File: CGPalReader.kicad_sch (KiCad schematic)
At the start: 27 parts, among them J1 Conn_01x06, U1 74LS14, U2 74LS393, U3 74LS393, U4 74LS151, U5 74LS393, U6 74LS151, U7 74LS157, U8 PAL16L8, U9 PAL20L10

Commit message: Add files via upload
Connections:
- net GND: now also U6.1 (I3), U6.12 (I7), U6.13 (I6), U6.14 (I5), U6.15 (I4)
- no-connect marks 21 -> 16
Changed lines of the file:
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@@
   (junction (at 109.22 144.272) (diameter 0) (color 0 0 0 0)
   )
+  (junction (at 238.76 171.196) (diameter 0) (color 0 0 0 0)
+  )
   (junction (at 230.124 140.716) (diameter 0) (color 0 0 0 0)
   )
@@
   (junction (at 158.75 235.712) (diameter 0) (color 0 0 0 0)
   )
+  (junction (at 238.76 148.336) (diameter 0) (color 0 0 0 0)
+  )
+  (junction (at 238.76 153.416) (diameter 0) (color 0 0 0 0)
+  )
   (junction (at 187.706 243.332) (diameter 0) (color 0 0 0 0)
   )
@@
   (junction (at 251.206 117.602) (diameter 0) (color 0 0 0 0)
   )
+  (junction (at 238.76 150.876) (diameter 0) (color 0 0 0 0)
+  )
   (junction (at 178.308 235.712) (diameter 0) (color 0 0 0 0)
   )
@@
   (junction (at 73.914 253.746) (diameter 0) (color 0 0 0 0)
   )
+  (junction (at 238.76 155.956) (diameter 0) (color 0 0 0 0)
+  )
   (junction (at 158.75 243.332) (diameter 0) (color 0 0 0 0)
   )
@@
   )
   (no_connect (at 363.982 62.738))
-  (no_connect (at 238.76 153.416))
   (no_connect (at 264.16 140.716))
   (no_connect (at 338.582 57.658))
   (no_connect (at 263.906 79.502))
   (no_connect (at 338.582 55.118))
-  (no_connect (at 238.76 145.796))
   (no_connect (at 363.982 55.118))
   (no_connect (at 30.48 174.498))
   (no_connect (at 274.828 249.174))
-  (no_connect (at 238.76 150.876))
   (no_connect (at 338.582 62.738))
-  (no_connect (at 238.76 155.956))
   (no_connect (at 338.582 50.038))
   (no_connect (at 338.582 47.498))
@@
   (no_connect (at 274.828 236.474))
   (no_connect (at 363.982 47.498))
-  (no_connect (at 238.76 148.336))
   (no_connect (at 338.582 65.278))
   (no_connect (at 297.942 249.428))
@@
     (stroke (width 0) (type default) (color 0 0 0 0))
   )
+  (wire (pts (xy 238.76 145.796) (xy 238.76 148.336))
+    (stroke (width 0) (type default) (color 0 0 0 0))
+  )
+  (wire (pts (xy 230.124 155.956) (xy 230.124 171.196))
+    (stroke (width 0) (type default) (color 0 0 0 0))
+  )
   (wire (pts (xy 148.336 172.466) (xy 122.936 172.466))
     (stroke (width 0) (type default) (color 0 0 0 0))
@@
     (stroke (width 0) (type default) (color 0 0 0 0))
   )
+  (wire (pts (xy 238.76 153.416) (xy 238.76 155.956))
+    (stroke (width 0) (type default) (color 0 0 0 0))
+  )
   (wire (pts (xy 230.124 131.572) (xy 230.124 140.716))
     (stroke (width 0) (type default) (color 0 0 0 0))
@@
     (stroke (width 0) (type default) (color 0 0 0 0))
   )
+  (wire (pts (xy 230.124 171.196) (xy 238.76 171.196))
+    (stroke (width 0) (type default) (color 0 0 0 0))
+  )
   (wire (pts (xy 231.14 59.944) (xy 231.14 92.202))
     (stroke (width 0) (type default) (color 0 0 0 0))
@@
     (stroke (width 0) (type default) (color 0 0 0 0))
   )
+  (wire (pts (xy 238.76 155.956) (xy 230.124 155.956))
+    (stroke (width 0) (type default) (color 0 0 0 0))
+  )
   (wire (pts (xy 338.582 80.518) (xy 351.282 80.518))
     (stroke (width 0) (type default) (color 0 0 0 0))
@@
     (stroke (width 0) (type default) (color 0 0 0 0))
   )
+  (wire (pts (xy 238.76 148.336) (xy 238.76 150.876))
+    (stroke (width 0) (type default) (color 0 0 0 0))
+  )
   (wire (pts (xy 213.614 79.502) (xy 238.506 79.502))
     (stroke (width 0) (type default) (color 0 0 0 0))
@@
     (stroke (width 0) (type default) (color 0 0 0 0))
   )
+  (wire (pts (xy 238.76 150.876) (xy 238.76 153.416))
+    (stroke (width 0) (type default) (color 0 0 0 0))
+  )

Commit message: Add files via upload
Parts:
- J1: footprint (none) -> Connector_PinHeader_2.54mm:PinHeader_1x06_P2.54mm_Vertical
- U1, U2, U3, U5: footprint (none) -> Package_DIP:DIP-14_W7.62mm_Socket_LongPads
- U4, U6, U7: footprint (none) -> Package_DIP:DIP-16_W7.62mm_Socket_LongPads
- U8: footprint (none) -> Package_DIP:DIP-20_W7.62mm_Socket_LongPads

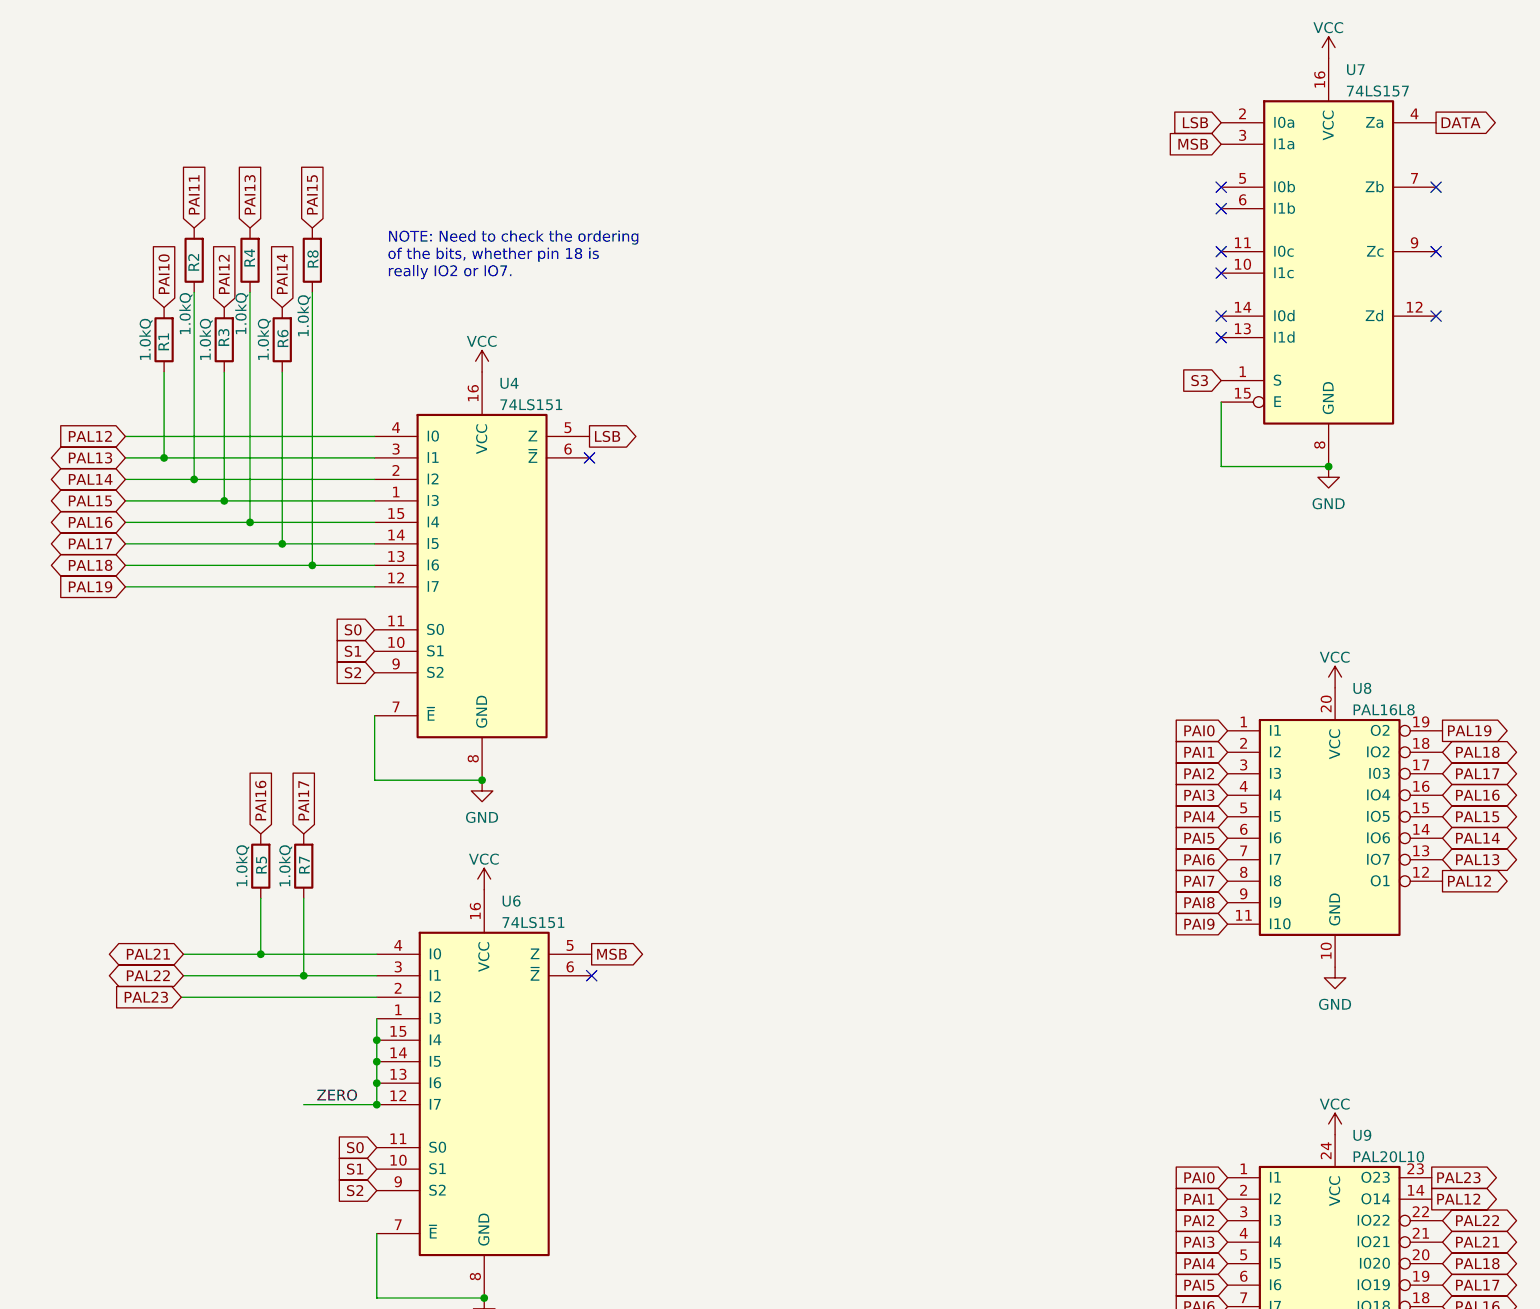
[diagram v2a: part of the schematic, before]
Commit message: Add files via upload
Changed input pin ordering.
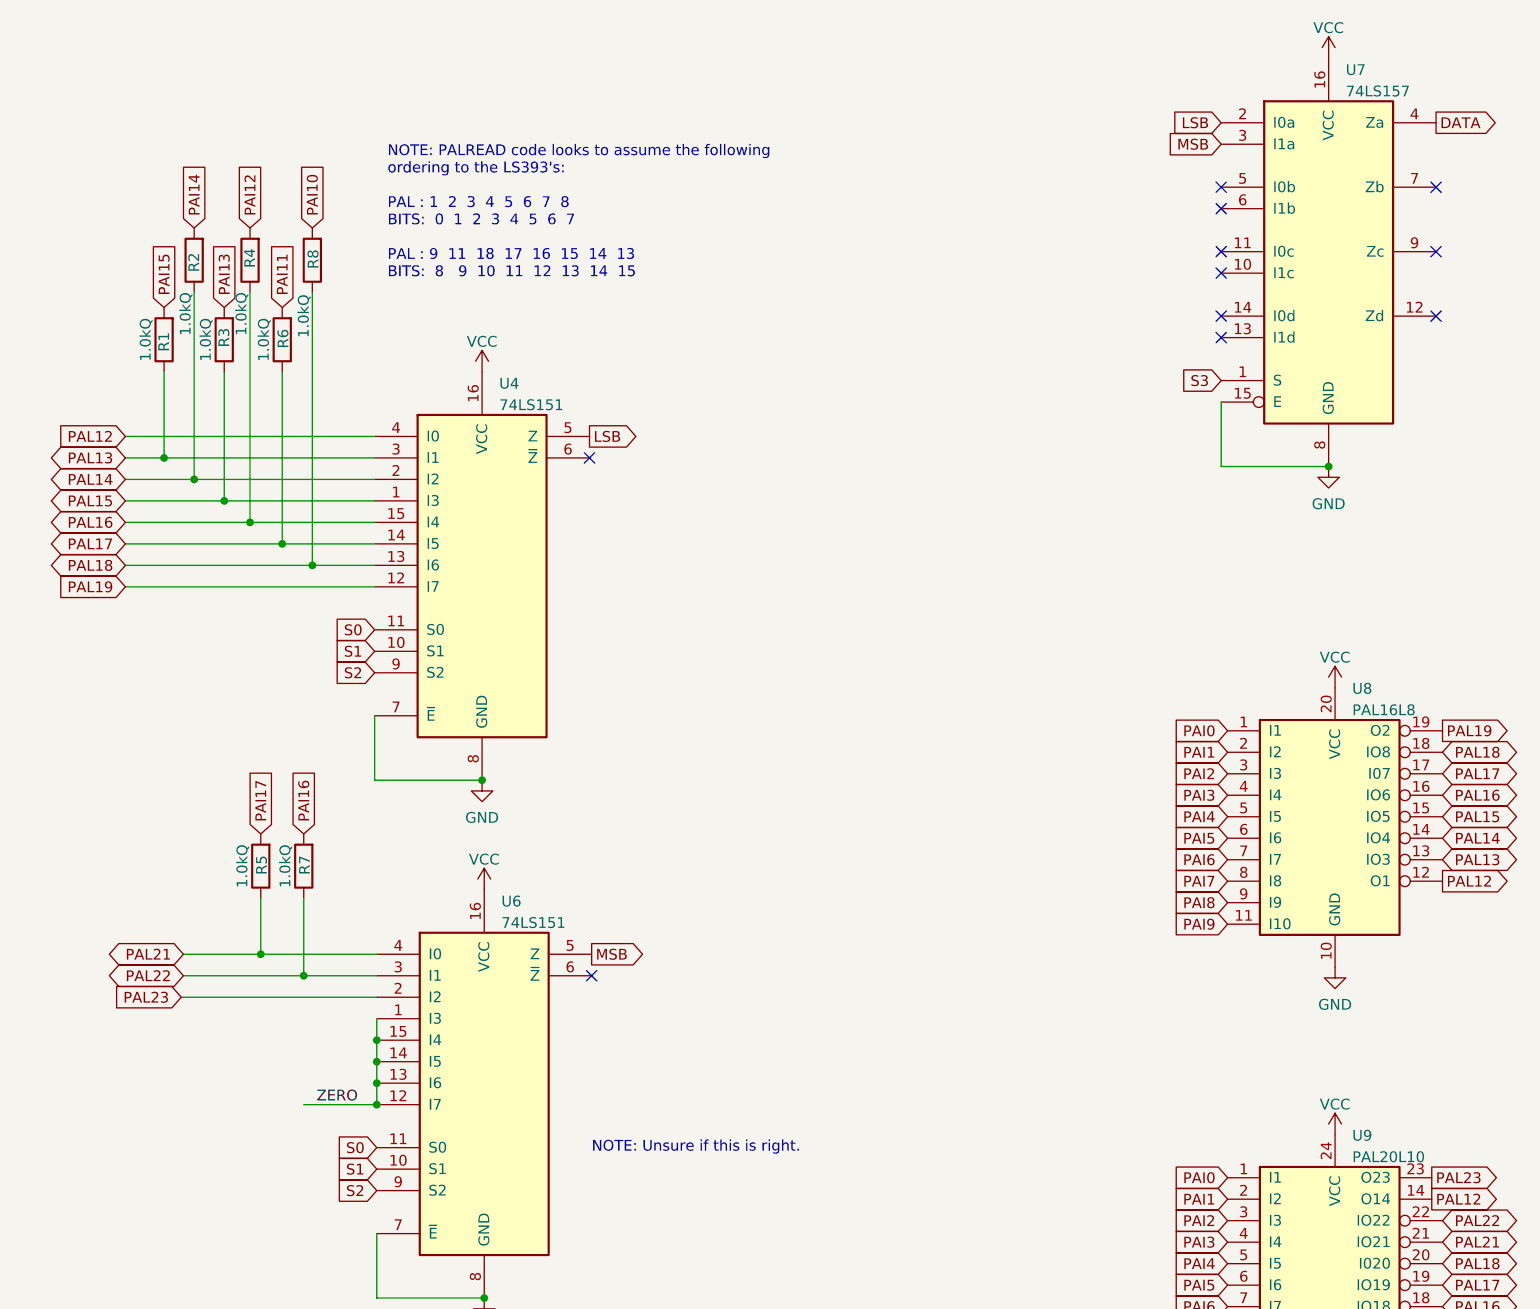
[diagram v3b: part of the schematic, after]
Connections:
- net PAI10: now also R8.2; no longer R1.2
- net PAI11: now also R6.2; no longer R2.2
- net PAI12: now also R4.2; no longer R3.2
- net PAI13: now also R3.2; no longer R4.2
- net PAI14: now also R2.2; no longer R6.2
- net PAI15: now also R1.2; no longer R8.2
- net PAI16: now also R7.2; no longer R5.2
- net PAI17: now also R5.2; no longer R7.2
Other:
- note added: "NOTE: PALREAD code looks to assume the following ordering to the LS393's: PAL : 1 2 3 4 5 6 7 8 BITS: 0 1 2 3 4 5 6 7 PAL : 9 11 18 17 16 15 14 13 BITS: 8 9 10 11 12 13 14 15"
- note added: "NOTE: Unsure if this is right."
- note removed: "NOTE: Need to check the ordering of the bits, whether pin 18 is really IO2 or IO7."
